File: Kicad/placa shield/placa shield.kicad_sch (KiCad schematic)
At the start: 20 parts, among them J1 HC-05 connector, J2 Digital/PWM, J3 Power, J4 Analog, J5 Digital/PWM, J6 Conn_01x05_Pin, SW1 SW_Push, SW2 SW_Push, SW3 SW_Push, SW4 SW_Push, SW5 SW_DIP_x04

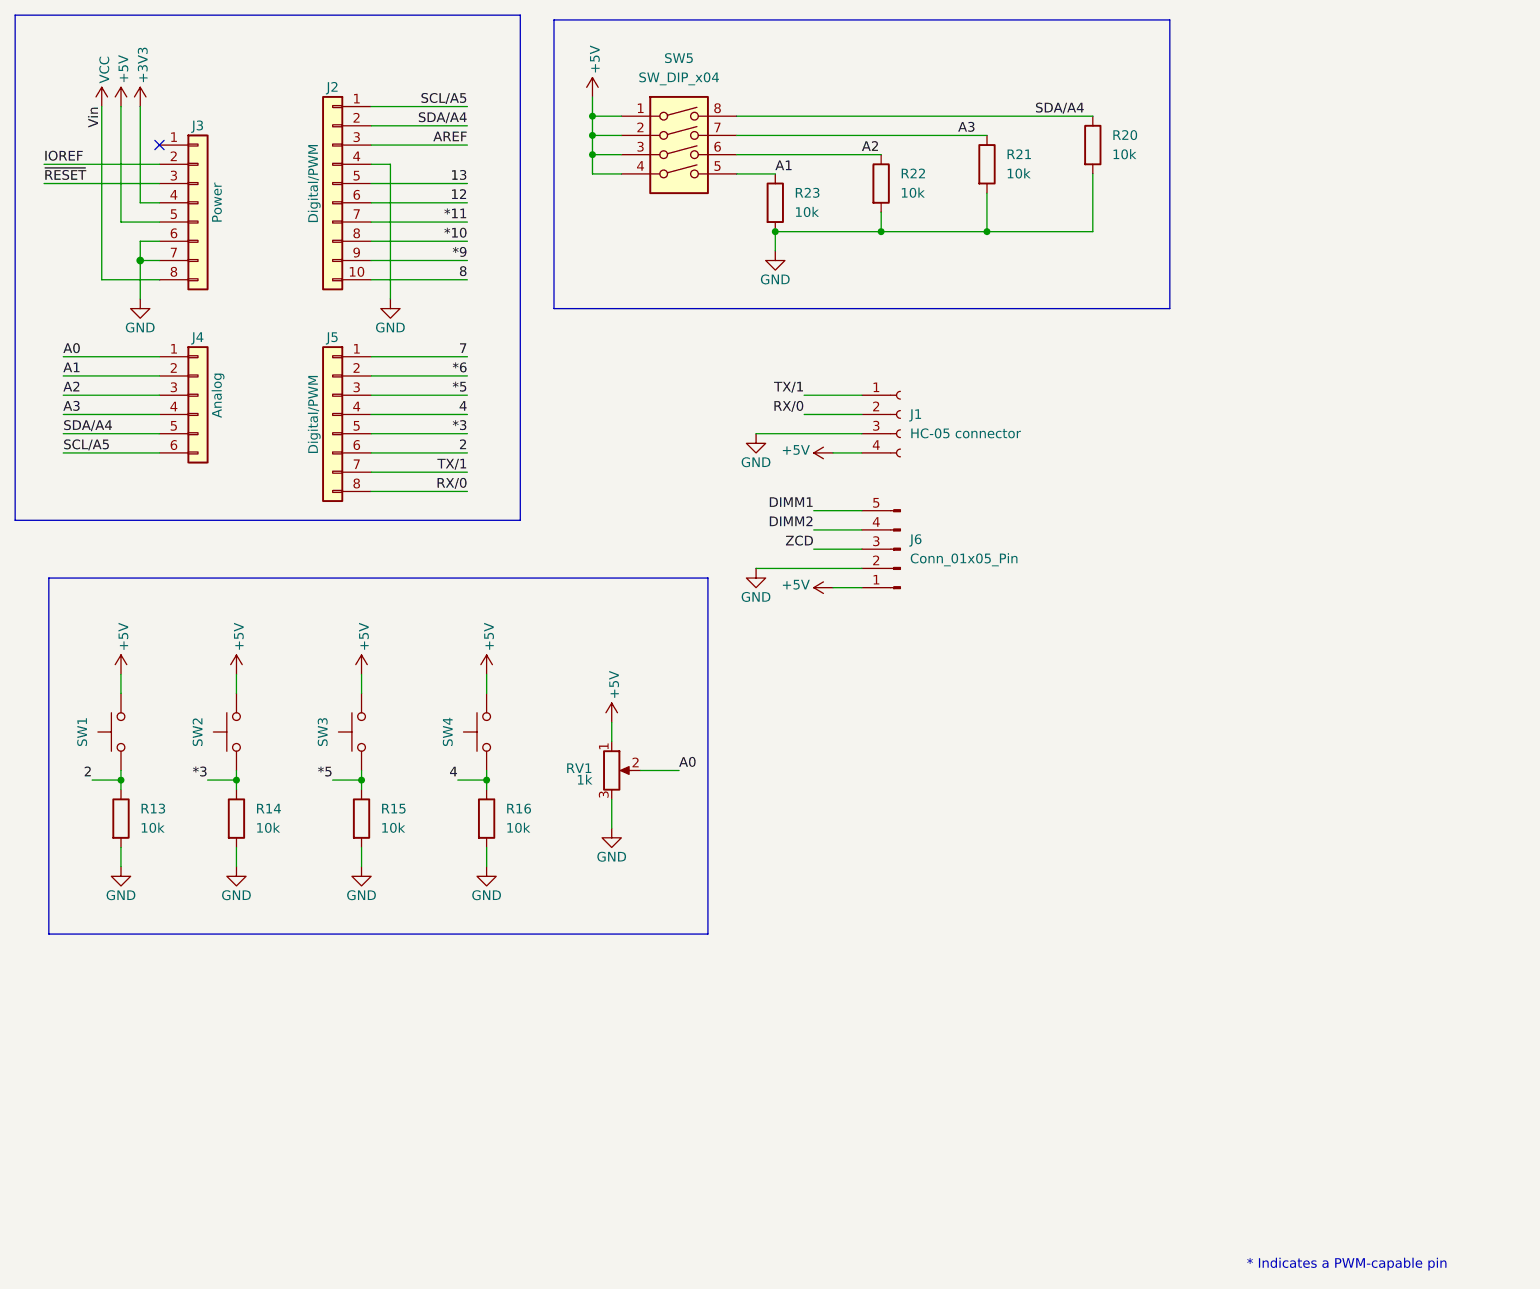
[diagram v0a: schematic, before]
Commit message: shield acomodado
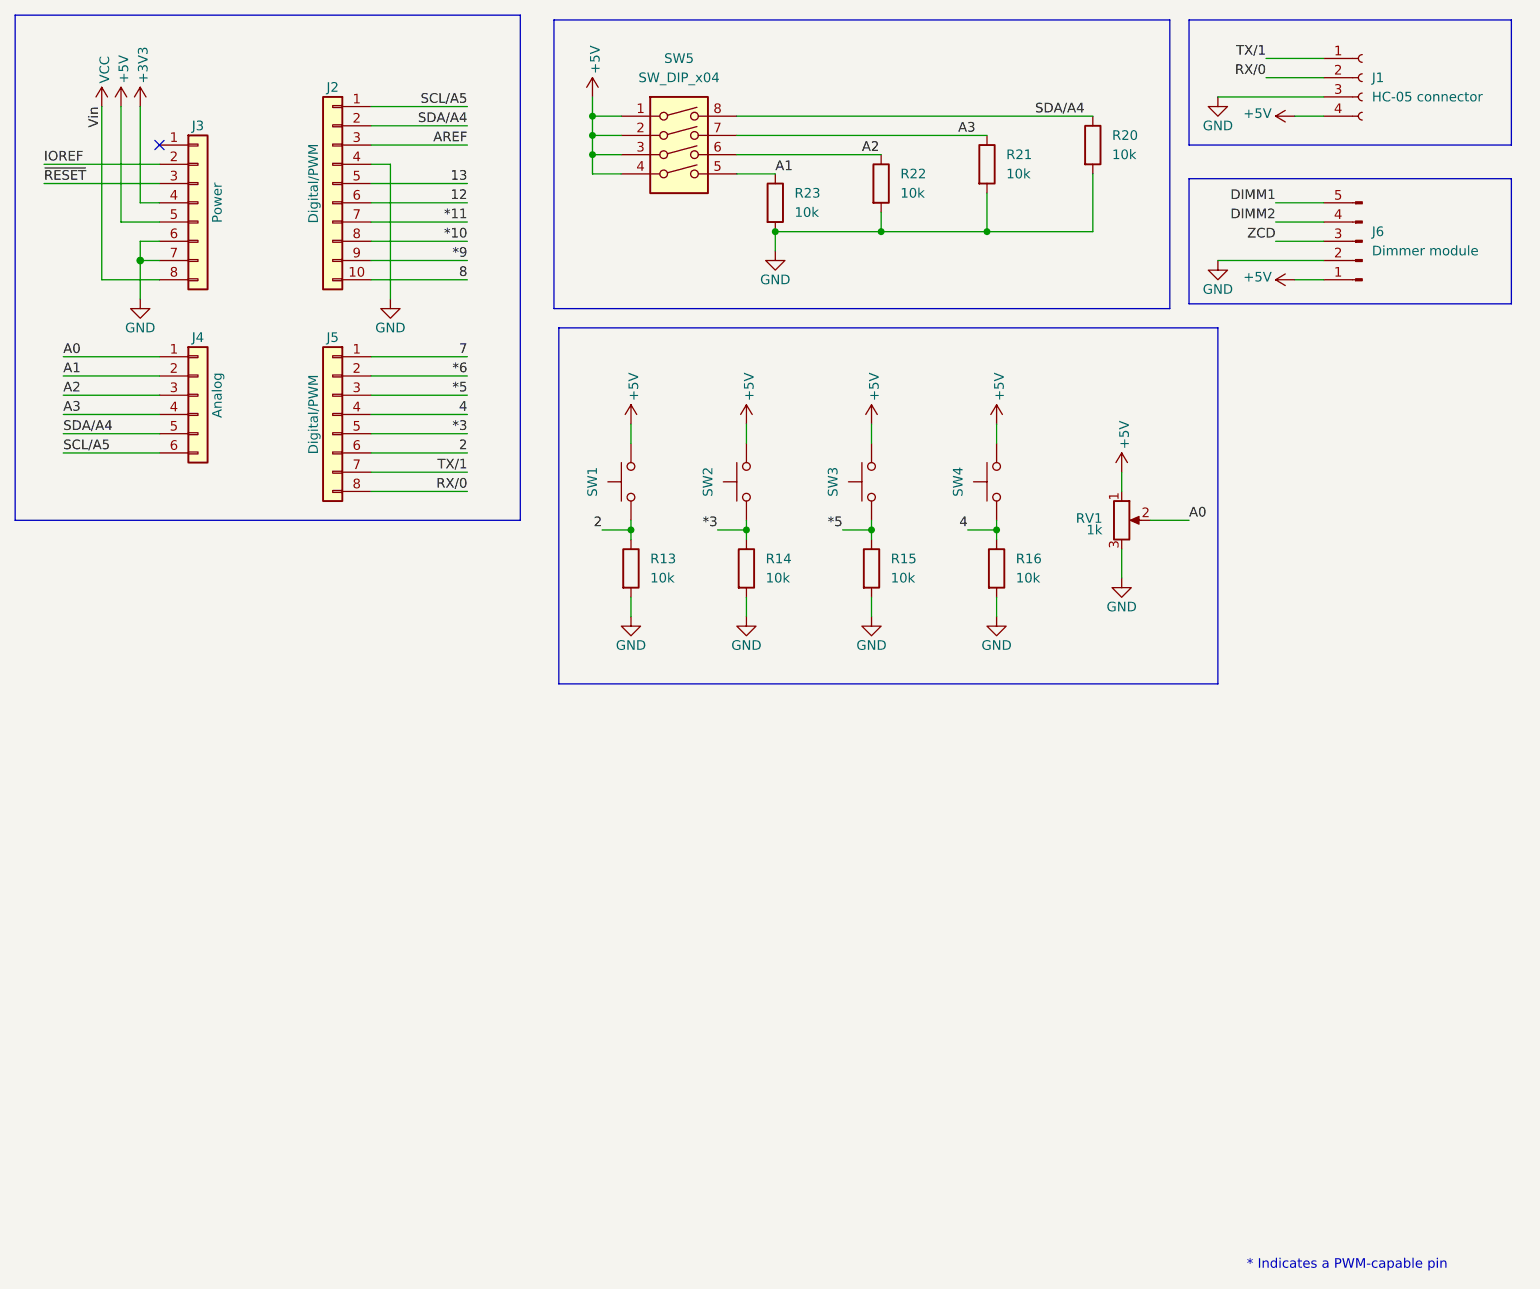
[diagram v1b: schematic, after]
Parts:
- J6: value Conn_01x05_Pin -> Dimmer module
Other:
- moved on the sheet: J1, J6, R13, R14, R15, R16, RV1, SW1, SW2, SW3, SW4
